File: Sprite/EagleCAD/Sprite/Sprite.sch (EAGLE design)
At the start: 23 parts, among them Q1 26MHz, U1 CC430F5137, U2 HMC5883LSMD, U3 ITG-3200

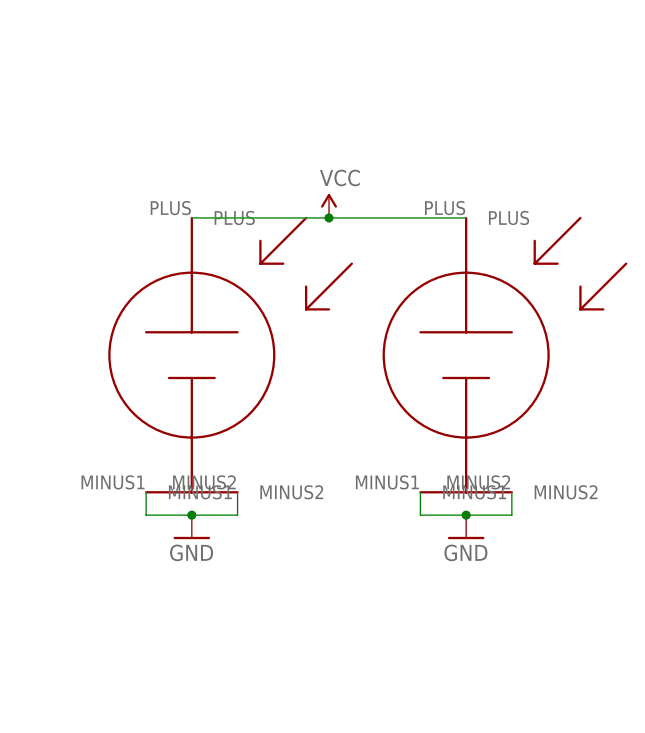
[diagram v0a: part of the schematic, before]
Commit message: Revert "Revert "Moved GND strip closer to TASC cells + removed bottom cells""
This reverts commit 1dc39e584056e569c73cdb2ce6a50d93971a399e.
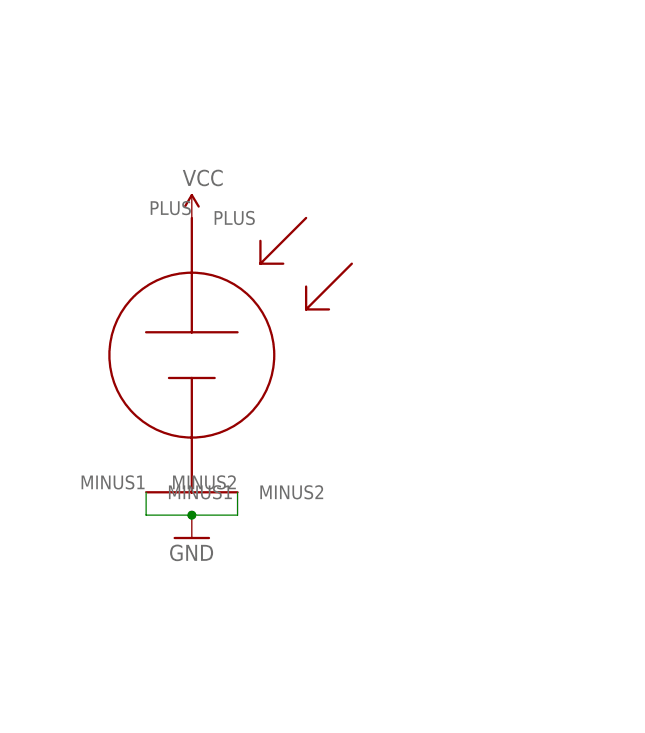
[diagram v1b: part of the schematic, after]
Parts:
- removed S2: TASC, TASC:TASC
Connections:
- net GND: no longer S2.MINUS1, S2.MINUS2
- net VCC: no longer S2.PLUS
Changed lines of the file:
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@@
 <parts>
 <part name="S1" library="TASC" deviceset="TASC" device=""/>
-<part name="S2" library="TASC" deviceset="TASC" device=""/>
 <part name="GND1" library="SparkFun" deviceset="GND" device=""/>
 <part name="P+1" library="SparkFun" deviceset="VCC" device=""/>
-<part name="GND2" library="SparkFun" deviceset="GND" device=""/>
 <part name="U1" library="TI_MSP430_v16" deviceset="CC430F513X---RGZ48" device="" value="CC430F5137"/>
 <part name="Q1" library="ABM11_JAA" deviceset="ABM11_CERAMIC_SMD_CRYSTAL" device="ABM11" value="26MHz"/>
@@
 <instances>
 <instance part="S1" gate="G$1" x="360.68" y="86.36"/>
-<instance part="S2" gate="G$1" x="391.16" y="86.36"/>
 <instance part="GND1" gate="1" x="360.68" y="66.04"/>
-<instance part="P+1" gate="1" x="375.92" y="101.6"/>
-<instance part="GND2" gate="1" x="391.16" y="66.04"/>
+<instance part="P+1" gate="1" x="360.68" y="101.6"/>
 <instance part="U1" gate="G$1" x="152.4" y="86.36"/>
 <instance part="Q1" gate="G$1" x="233.68" y="48.26" rot="R90"/>
@@
 <segment>
 <pinref part="S1" gate="G$1" pin="PLUS"/>
-<pinref part="S2" gate="G$1" pin="PLUS"/>
-<wire x1="360.68" y1="101.6" x2="375.92" y2="101.6" width="0.1524" layer="91"/>
 <pinref part="P+1" gate="1" pin="VCC"/>
-<wire x1="375.92" y1="101.6" x2="391.16" y2="101.6" width="0.1524" layer="91"/>
-<junction x="375.92" y="101.6"/>
 </segment>
 <segment>
@@
 </segment>
 <segment>
-<pinref part="GND2" gate="1" pin="GND"/>
-<pinref part="S2" gate="G$1" pin="MINUS1"/>
-<wire x1="391.16" y1="68.58" x2="386.08" y2="68.58" width="0.1524" layer="91"/>
-<wire x1="386.08" y1="68.58" x2="386.08" y2="71.12" width="0.1524" layer="91"/>
-<pinref part="S2" gate="G$1" pin="MINUS2"/>
-<wire x1="391.16" y1="68.58" x2="396.24" y2="68.58" width="0.1524" layer="91"/>
-<wire x1="396.24" y1="68.58" x2="396.24" y2="71.12" width="0.1524" layer="91"/>
-<junction x="391.16" y="68.58"/>
-</segment>
-<segment>

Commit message: Revert "Moved GND strip closer to TASC cells + removed bottom cells"
This reverts commit a51b0ba4fb3e3dccbe7975012f3db8ac667cb900.
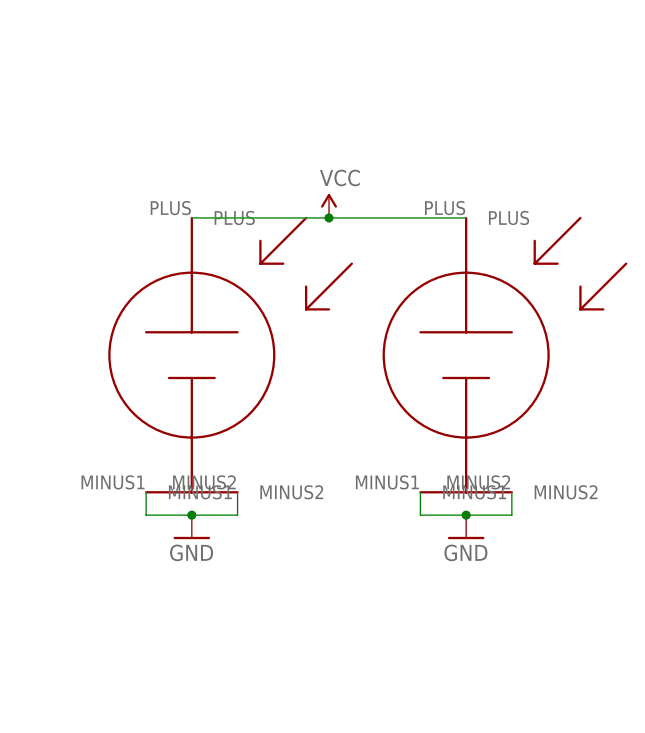
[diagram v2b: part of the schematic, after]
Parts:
- added S2: TASC, TASC:TASC
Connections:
- net GND: now also S2.MINUS1, S2.MINUS2
- net VCC: now also S2.PLUS
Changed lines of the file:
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@@
 <parts>
 <part name="S1" library="TASC" deviceset="TASC" device=""/>
+<part name="S2" library="TASC" deviceset="TASC" device=""/>
 <part name="GND1" library="SparkFun" deviceset="GND" device=""/>
 <part name="P+1" library="SparkFun" deviceset="VCC" device=""/>
+<part name="GND2" library="SparkFun" deviceset="GND" device=""/>
 <part name="U1" library="TI_MSP430_v16" deviceset="CC430F513X---RGZ48" device="" value="CC430F5137"/>
 <part name="Q1" library="ABM11_JAA" deviceset="ABM11_CERAMIC_SMD_CRYSTAL" device="ABM11" value="26MHz"/>
@@
 <instances>
 <instance part="S1" gate="G$1" x="360.68" y="86.36"/>
+<instance part="S2" gate="G$1" x="391.16" y="86.36"/>
 <instance part="GND1" gate="1" x="360.68" y="66.04"/>
-<instance part="P+1" gate="1" x="360.68" y="101.6"/>
+<instance part="P+1" gate="1" x="375.92" y="101.6"/>
+<instance part="GND2" gate="1" x="391.16" y="66.04"/>
 <instance part="U1" gate="G$1" x="152.4" y="86.36"/>
 <instance part="Q1" gate="G$1" x="233.68" y="48.26" rot="R90"/>
@@
 <segment>
 <pinref part="S1" gate="G$1" pin="PLUS"/>
+<pinref part="S2" gate="G$1" pin="PLUS"/>
+<wire x1="360.68" y1="101.6" x2="375.92" y2="101.6" width="0.1524" layer="91"/>
 <pinref part="P+1" gate="1" pin="VCC"/>
+<wire x1="375.92" y1="101.6" x2="391.16" y2="101.6" width="0.1524" layer="91"/>
+<junction x="375.92" y="101.6"/>
 </segment>
 <segment>
@@
 </segment>
 <segment>
+<pinref part="GND2" gate="1" pin="GND"/>
+<pinref part="S2" gate="G$1" pin="MINUS1"/>
+<wire x1="391.16" y1="68.58" x2="386.08" y2="68.58" width="0.1524" layer="91"/>
+<wire x1="386.08" y1="68.58" x2="386.08" y2="71.12" width="0.1524" layer="91"/>
+<pinref part="S2" gate="G$1" pin="MINUS2"/>
+<wire x1="391.16" y1="68.58" x2="396.24" y2="68.58" width="0.1524" layer="91"/>
+<wire x1="396.24" y1="68.58" x2="396.24" y2="71.12" width="0.1524" layer="91"/>
+<junction x="391.16" y="68.58"/>
+</segment>
+<segment>
